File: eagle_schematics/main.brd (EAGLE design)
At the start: 100 x 80 mm, 10 parts, among them IC1 MEGA8-P

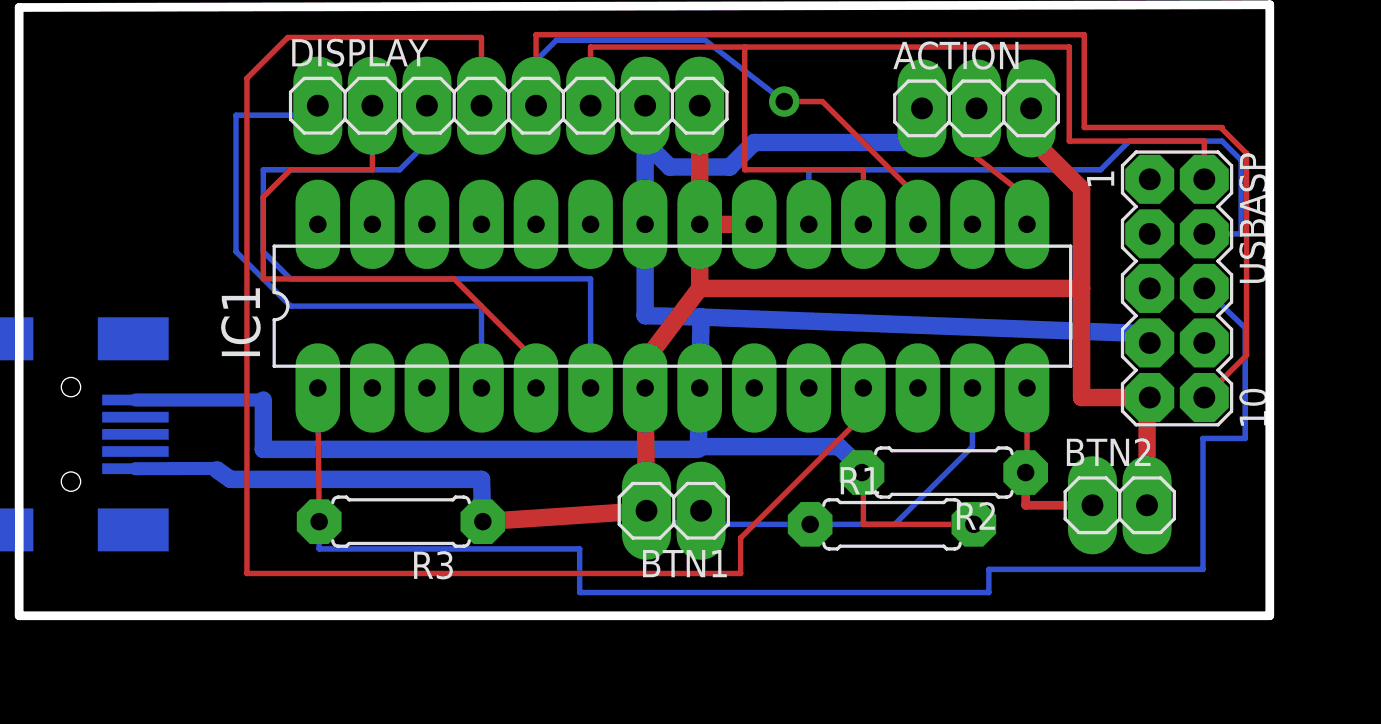
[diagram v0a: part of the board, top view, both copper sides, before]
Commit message: fix bug in schematics, change pump pin
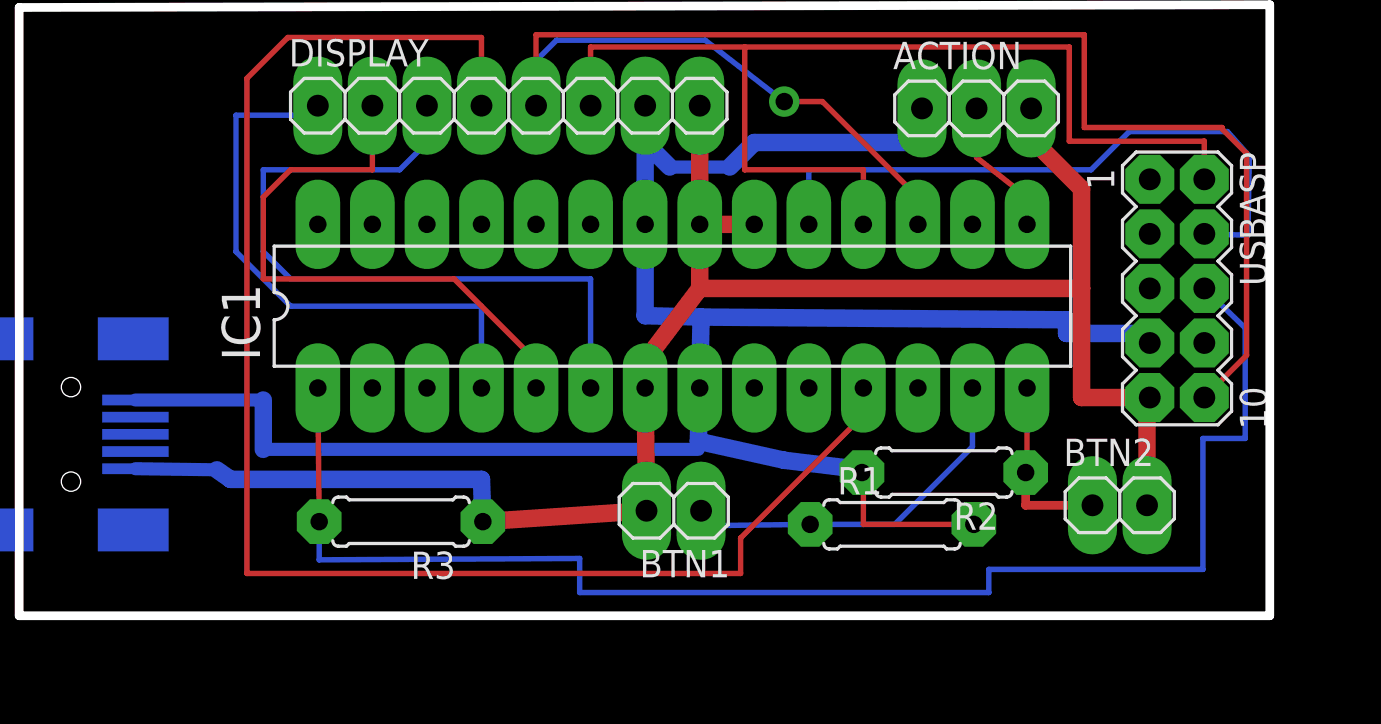
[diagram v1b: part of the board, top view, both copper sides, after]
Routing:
- net PD7: track 19.7 -> 17.6 mm
- net SCK: track 28.7 -> 30.0 mm
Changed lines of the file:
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@@
 <wire x1="45.72" y1="48.26" x2="53.5305" y2="48.26" width="0.8128" layer="16"/>
 <wire x1="44.577" y1="47.117" x2="45.72" y2="48.26" width="0.8128" layer="16"/>
-<wire x1="41.783" y1="47.117" x2="44.577" y2="47.117" width="0.8128" layer="16"/>
+<wire x1="41.783" y1="47.117" x2="44.577" y2="47.117" width="0.6096" layer="16"/>
 <wire x1="40.64" y1="48.26" x2="41.783" y2="47.117" width="0.8128" layer="16"/>
 <wire x1="40.64" y1="49.9745" x2="40.64" y2="48.26" width="0.254" layer="16"/>
@@
 <wire x1="43.2435" y1="40.132" x2="43.18" y2="36.83" width="0.8128" layer="16"/>
 <wire x1="64.135" y1="38.9255" x2="63.6905" y2="39.37" width="0.254" layer="16"/>
-<wire x1="63.6905" y1="39.37" x2="43.2435" y2="40.132" width="0.8128" layer="16"/>
-<wire x1="49.657" y1="34.0995" x2="50.8" y2="33.02" width="0.8128" layer="16"/>
-<wire x1="43.1165" y1="34.0995" x2="49.657" y2="34.0995" width="0.8128" layer="16"/>
+<wire x1="63.6905" y1="39.37" x2="60.2615" y2="39.37" width="0.8128" layer="16"/>
+<wire x1="60.2615" y1="39.37" x2="60.2615" y2="40.005" width="0.8128" layer="16"/>
+<wire x1="60.2615" y1="40.005" x2="43.2435" y2="40.132" width="0.8128" layer="16"/>
+<wire x1="47.117" y1="33.4645" x2="50.8" y2="33.02" width="0.8128" layer="16"/>
+<wire x1="43.1165" y1="34.3535" x2="47.117" y2="33.4645" width="0.8128" layer="16"/>
 <wire x1="50.8" y1="33.02" x2="50.7365" y2="32.893" width="0.254" layer="16"/>
 <wire x1="40.64" y1="40.1955" x2="40.64" y2="44.45" width="0.8128" layer="16"/>
@@
 <wire x1="16.9065" y1="36.271" x2="22.86" y2="36.271" width="0.6096" layer="16"/>
 <wire x1="22.86" y1="36.271" x2="22.86" y2="33.9725" width="0.8128" layer="16"/>
-<wire x1="22.86" y1="33.9725" x2="43.1165" y2="33.9725" width="0.8128" layer="16"/>
-<wire x1="43.1165" y1="33.9725" x2="43.1165" y2="34.0995" width="0.4064" layer="16"/>
-<wire x1="43.1165" y1="34.0995" x2="43.18" y2="36.83" width="0.8128" layer="16"/>
+<wire x1="22.86" y1="33.9725" x2="43.1165" y2="33.9725" width="0.6096" layer="16"/>
+<wire x1="43.1165" y1="33.9725" x2="43.1165" y2="34.3535" width="0.4064" layer="16"/>
+<wire x1="43.1165" y1="34.3535" x2="43.18" y2="36.83" width="0.8128" layer="16"/>
 <polygon width="0.4064" layer="16">
 <vertex x="11.4935" y="54.4195"/>
@@
 <wire x1="33.02" y1="32.5755" x2="21.336" y2="32.5755" width="0.8128" layer="16"/>
 <wire x1="21.336" y1="32.5755" x2="20.701" y2="33.02" width="0.8128" layer="16"/>
-<wire x1="20.701" y1="33.02" x2="20.78" y2="33.0835" width="0.6096" layer="16"/>
-<wire x1="20.78" y1="33.0835" x2="16.9065" y2="33.071" width="0.6096" layer="16"/>
+<wire x1="20.701" y1="33.02" x2="20.78" y2="33.02" width="0.6096" layer="16"/>
+<wire x1="20.78" y1="33.02" x2="16.9065" y2="33.071" width="0.6096" layer="16"/>
 <wire x1="64.135" y1="36.3855" x2="64.008" y2="36.3855" width="0.4064" layer="16"/>
 <wire x1="64.008" y1="36.3855" x2="64.008" y2="31.369" width="0.8128" layer="1"/>
@@
 <contactref element="IC1" pad="13"/>
 <contactref element="BTN1" pad="1"/>
-<wire x1="41.91" y1="30.48" x2="48.3235" y2="30.48" width="0.254" layer="16"/>
-<wire x1="43.2435" y1="31.115" x2="41.91" y2="30.48" width="0.254" layer="16"/>
+<wire x1="43.2435" y1="30.4165" x2="48.3235" y2="30.48" width="0.254" layer="16"/>
+<wire x1="43.2435" y1="31.115" x2="43.2435" y2="30.4165" width="0.254" layer="16"/>
 <wire x1="52.2605" y1="30.48" x2="48.3235" y2="30.48" width="0.254" layer="16"/>
 <wire x1="55.88" y1="34.0995" x2="55.88" y2="36.83" width="0.254" layer="16"/>
@@
 <wire x1="66.6115" y1="28.3845" x2="66.6115" y2="34.4805" width="0.254" layer="16"/>
 <wire x1="66.6115" y1="34.4805" x2="68.58" y2="34.4805" width="0.254" layer="16"/>
-<wire x1="25.4635" y1="30.607" x2="25.4635" y2="29.337" width="0.254" layer="16"/>
-<wire x1="25.4635" y1="29.337" x2="37.592" y2="29.337" width="0.254" layer="16"/>
-<wire x1="37.592" y1="29.337" x2="37.592" y2="27.305" width="0.254" layer="16"/>
+<wire x1="25.4635" y1="30.607" x2="25.4635" y2="28.829" width="0.254" layer="16"/>
+<wire x1="25.4635" y1="28.829" x2="37.592" y2="28.8925" width="0.254" layer="16"/>
+<wire x1="37.592" y1="28.8925" x2="37.592" y2="27.305" width="0.254" layer="16"/>
 </signal>
 <signal name="SCK">
@@
 <contactref element="USBASP" pad="4"/>
 <wire x1="48.26" y1="46.99" x2="48.26" y2="44.45" width="0.254" layer="16"/>
-<wire x1="61.849" y1="46.99" x2="48.26" y2="46.99" width="0.254" layer="16"/>
-<wire x1="63.1825" y1="48.3235" x2="61.849" y2="46.99" width="0.254" layer="16"/>
-<wire x1="67.5005" y1="48.3235" x2="63.1825" y2="48.3235" width="0.254" layer="16"/>
-<wire x1="68.3895" y1="47.4345" x2="67.5005" y2="48.3235" width="0.254" layer="16"/>
-<wire x1="68.3895" y1="44.0055" x2="68.3895" y2="47.4345" width="0.254" layer="16"/>
-<wire x1="66.675" y1="44.0055" x2="68.3895" y2="44.0055" width="0.254" layer="16"/>
+<wire x1="61.4045" y1="46.99" x2="48.26" y2="46.99" width="0.254" layer="16"/>
+<wire x1="63.1825" y1="48.768" x2="61.4045" y2="46.99" width="0.254" layer="16"/>
+<wire x1="67.7545" y1="48.768" x2="63.1825" y2="48.768" width="0.254" layer="16"/>
+<wire x1="68.7705" y1="47.625" x2="67.7545" y2="48.768" width="0.254" layer="16"/>
+<wire x1="68.707" y1="43.942" x2="68.7705" y2="47.625" width="0.254" layer="16"/>
+<wire x1="66.675" y1="44.0055" x2="68.707" y2="43.942" width="0.254" layer="16"/>
 </signal>
 <signal name="PB1">
